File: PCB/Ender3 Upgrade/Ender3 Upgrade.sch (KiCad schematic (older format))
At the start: 1 part

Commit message: PCB Designed
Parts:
- added C1, C2, C3, C4, C5, C6, C7, C8: Conn_01x02, Connector_JST:JST_EH_B2B-EH-A_1x02_P2.50mm_Vertical, symbol Connector_Generic:Conn_01x02
- added DCDCBC2: DCDC 24-12, albe:BuckConverter, symbol Alberto:DCDCBuckConverter
- added J1, J2: Conn_01x04_Male, Connector_PinSocket_2.54mm:PinSocket_1x04_P2.54mm_Vertical, symbol Connector:Conn_01x04_Male
- added J3: Conn_01x02_Female, symbol Connector:Conn_01x02_Female
- added R1, R2, R3, R4, R5, R6, R7, R8: R1, Resistor_THT:R_Axial_DIN0204_L3.6mm_D1.6mm_P7.62mm_Horizontal, symbol Device:R
- added T1, T2, T3, T4, T5, T6, T7, T8: IRLZ34N, Package_TO_SOT_THT:TO-220-3_Vertical, symbol Transistor_FET:IRLZ34N
- DCDCBC1: value DCDCBuckConverter -> DCDC 24-5
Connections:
- net +24V: now also DCDCBC2.2 (IN+), J3.2 (Pin_2)
- net GND: now also DCDCBC1.3 (OUT-), DCDCBC2.3 (OUT-), R1.2, R2.2, R3.2, R4.2, R5.2, R6.2, R7.2, R8.2, T1.3 (S), T2.3 (S), T3.3 (S), T4.3 (S), T5.3 (S), T6.3 (S), T7.3 (S), T8.3 (S); no longer DCDCBC1.1 (IN-)
- net 5V: now reaches DCDCBC1.4 (OUT+)
- net 5V: now also C1.2 (Pin_2), C3.2 (Pin_2), C5.2 (Pin_2), C7.2 (Pin_2)
- new net: J1.4 (Pin_4), R1.1, T1.1 (G)
- new net: C1.1 (Pin_1), T1.2 (D)
- new net: C2.1 (Pin_1), T2.2 (D)
- new net: C4.1 (Pin_1), T4.2 (D)
- new net: C6.1 (Pin_1), T6.2 (D)
- new net: C8.1 (Pin_1), T8.2 (D)
- new net: J1.3 (Pin_3), R3.1, T3.1 (G)
- new net: C3.1 (Pin_1), T3.2 (D)
- new net: J1.2 (Pin_2), R5.1, T5.1 (G)
- new net: C5.1 (Pin_1), T5.2 (D)
- new net: J1.1 (Pin_1), R7.1, T7.1 (G)
- new net: C7.1 (Pin_1), T7.2 (D)
- new net: J2.4 (Pin_4), R8.1, T8.1 (G)
- new net: J2.3 (Pin_3), R6.1, T6.1 (G)
- new net: J2.2 (Pin_2), R4.1, T4.1 (G)
- new net: J2.1 (Pin_1), R2.1, T2.1 (G)
- new net 12V: C2.2 (Pin_2), C4.2 (Pin_2), C6.2 (Pin_2), C8.2 (Pin_2), DCDCBC2.4 (OUT+)
- new net GNDPWR: DCDCBC1.1 (IN-), DCDCBC2.1 (IN-), J3.1 (Pin_1)
- no-connect marks 0 -> 1

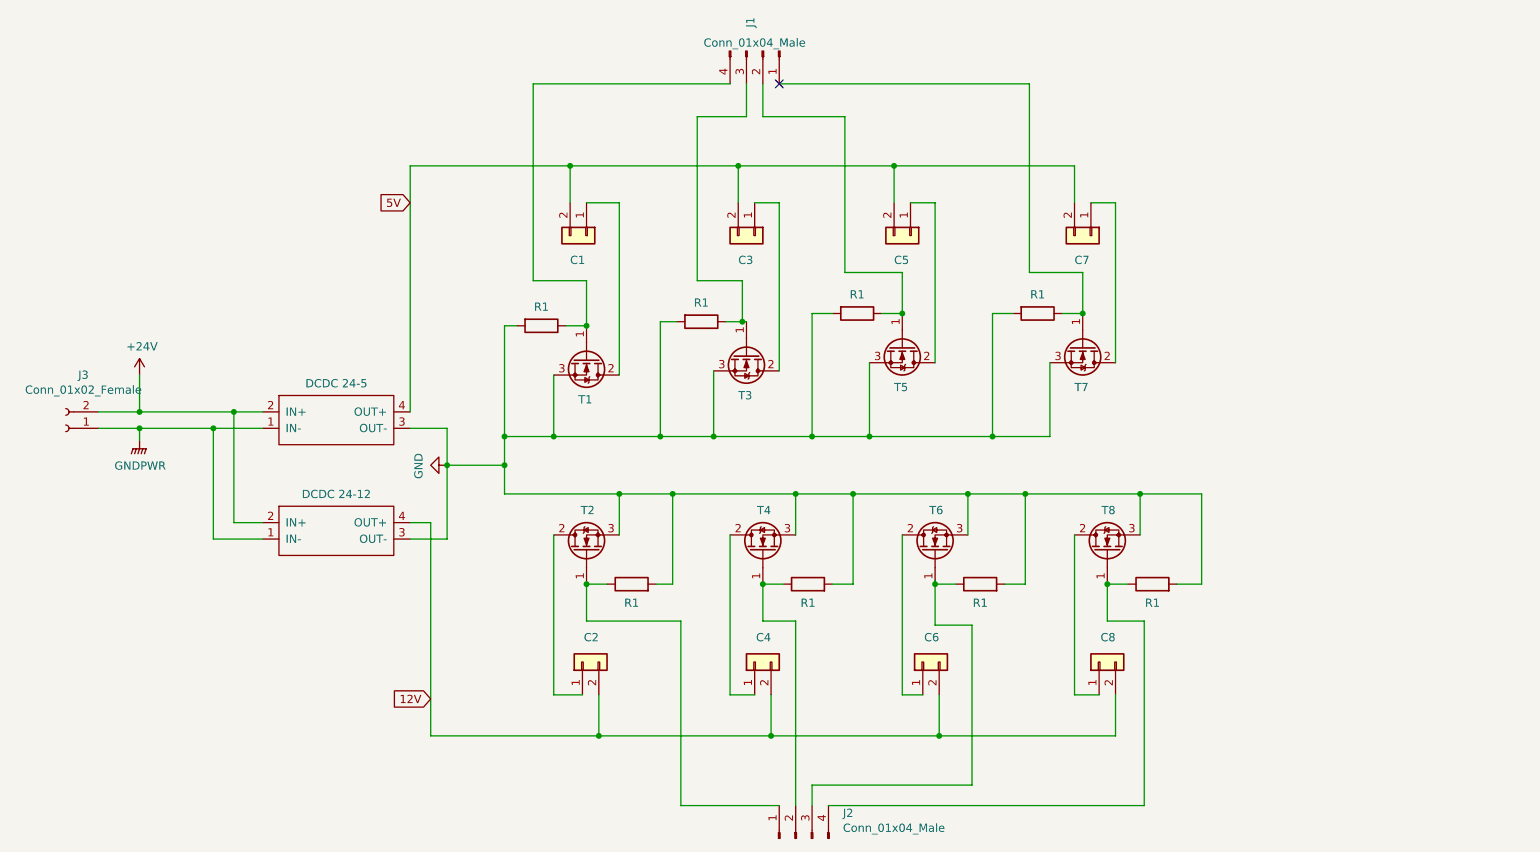
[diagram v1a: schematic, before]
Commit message: Drawers added
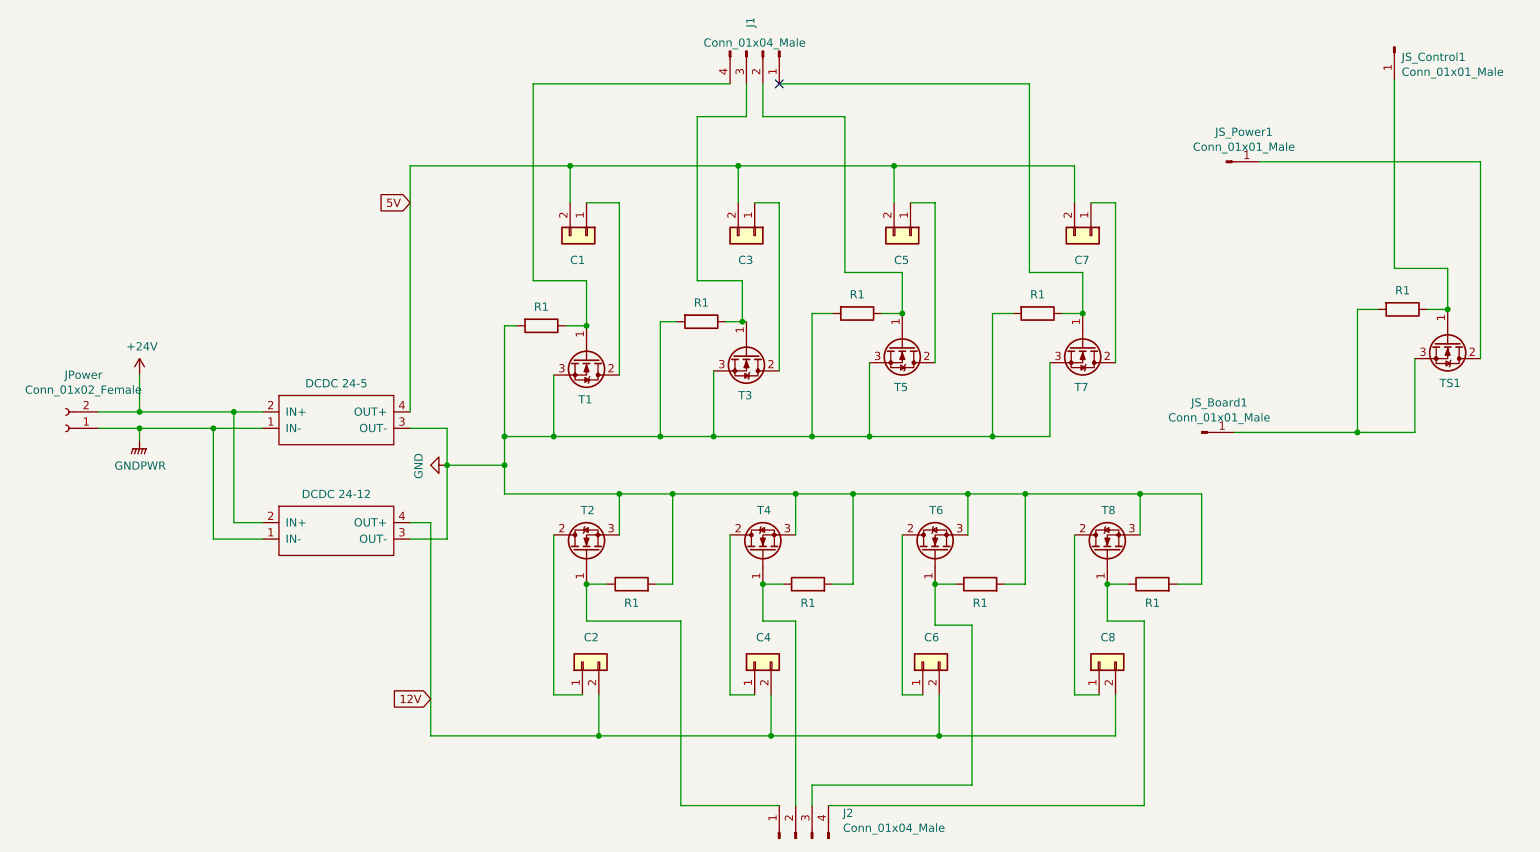
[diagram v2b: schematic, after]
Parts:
- removed J3: Conn_01x02_Female, symbol Connector:Conn_01x02_Female
- added JPower: Conn_01x02_Female, symbol Connector:Conn_01x02_Female
- added JS_Board1, JS_Control1, JS_Power1: Conn_01x01_Male, Connector_PinHeader_2.54mm:PinHeader_1x01_P2.54mm_Vertical, symbol Connector:Conn_01x01_Male
- added RS1: R1, Resistor_THT:R_Axial_DIN0204_L3.6mm_D1.6mm_P7.62mm_Horizontal, symbol Device:R
- added TS1: IRLZ34N, Package_TO_SOT_THT:TO-220-3_Vertical, symbol Transistor_FET:IRLZ34N
- J1, J2: footprint Connector_PinSocket_2.54mm:PinSocket_1x04_P2.54mm_Vertical -> Connector_PinHeader_2.54mm:PinHeader_1x04_P2.54mm_Vertical
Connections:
- net +24V: now also JPower.2 (Pin_2)
- net GNDPWR: now also JPower.1 (Pin_1)
- new net: JS_Power1.1 (Pin_1), TS1.2 (D)
- new net: JS_Board1.1 (Pin_1), RS1.2, TS1.3 (S)
- new net: JS_Control1.1 (Pin_1), RS1.1, TS1.1 (G)
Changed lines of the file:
@@
 F 0 "J2" V 5704 5712 50  0000 R CNN
 F 1 "Conn_01x04_Male" V 5613 5712 50  0000 R CNN
-F 2 "Connector_PinSocket_2.54mm:PinSocket_1x04_P2.54mm_Vertical" H 5550 6000 50  0001 C CNN
+F 2 "Connector_PinHeader_2.54mm:PinHeader_1x04_P2.54mm_Vertical" H 5550 6000 50  0001 C CNN
 F 3 "~" H 5550 6000 50  0001 C CNN
 	1    5550 6000
@@
 F 0 "J1" H 5175 1125 50  0000 C CNN
 F 1 "Conn_01x04_Male" V 5300 1150 50  0000 C CNN
-F 2 "Connector_PinSocket_2.54mm:PinSocket_1x04_P2.54mm_Vertical" H 5350 1200 50  0001 C CNN
+F 2 "Connector_PinHeader_2.54mm:PinHeader_1x04_P2.54mm_Vertical" H 5350 1200 50  0001 C CNN
 F 3 "~" H 5350 1200 50  0001 C CNN
 	1    5350 1200
@@
 	6975 1400 5450 1400
 Connection ~ 7300 2800
-$Comp
-L Connector:Conn_01x02_Female J3
-U 1 1 64084918
-P 1100 3500
-F 0 "J3" H 992 3175 50  0000 C CNN
-F 1 "Conn_01x02_Female" H 992 3266 50  0000 C CNN
-F 2 "" H 1100 3500 50  0001 C CNN
-F 3 "~" H 1100 3500 50  0001 C CNN
-	1    1100 3500
-	-1   0    0    1
-$EndComp
 Wire Wire Line
 	1300 3400 1550 3400
@@
 $EndComp
 NoConn ~ 5450 1400
+$Comp
+L Connector:Conn_01x01_Male JS_Power1
+U 1 1 6402B6DD
+P 8175 1875
+F 0 "JS_Power1" H 8283 2056 50  0000 C CNN
+F 1 "Conn_01x01_Male" H 8283 1965 50  0000 C CNN
+F 2 "Connector_PinHeader_2.54mm:PinHeader_1x01_P2.54mm_Vertical" H 8175 1875 50  0001 C CNN
+F 3 "~" H 8175 1875 50  0001 C CNN
+	1    8175 1875
+	1    0    0    -1
+$EndComp
+$Comp
+L Connector:Conn_01x01_Male JS_Board1
+U 1 1 64031B0D
+P 8025 3525
+F 0 "JS_Board1" H 8133 3706 50  0000 C CNN
+F 1 "Conn_01x01_Male" H 8133 3615 50  0000 C CNN
+F 2 "Connector_PinHeader_2.54mm:PinHeader_1x01_P2.54mm_Vertical" H 8025 3525 50  0001 C CNN
+F 3 "~" H 8025 3525 50  0001 C CNN
+	1    8025 3525
+	1    0    0    -1
+$EndComp
+$Comp
+L Transistor_FET:IRLZ34N TS1
+U 1 1 6403AD45
+P 9525 2975
+F 0 "TS1" V 9775 2925 50  0000 L CNN
+F 1 "IRLZ34N" H 9729 2930 50  0001 L CNN
+F 2 "Package_TO_SOT_THT:TO-220-3_Vertical" H 9775 2900 50  0001 L CIN
+F 3 "http://www.infineon.com/dgdl/irlz34npbf.pdf?fileId=5546d462533600a40153567206892720" H 9525 2975 50  0001 L CNN
+	1    9525 2975
+	0    1    1    0
+$EndComp
+$Comp
+L Device:R RS1
+U 1 1 6403B133
+P 9250 2775
+F 0 "RS1" V 9043 2775 50  0001 C CNN
+F 1 "R1" V 9135 2775 50  0000 C CNN
+F 2 "Resistor_THT:R_Axial_DIN0204_L3.6mm_D1.6mm_P7.62mm_Horizontal" V 9180 2775 50  0001 C CNN
+F 3 "~" H 9250 2775 50  0001 C CNN
+	1    9250 2775
+	0    1    1    0
+$EndComp
+Wire Wire Line
+	9525 2775 9400 2775
+Wire Wire Line
+	9325 3075 9325 3525
+Wire Wire Line
+	9325 3525 8975 3525
+Wire Wire Line
+	9100 2775 8975 2775
+Wire Wire Line
+	8975 2775 8975 3525
+Connection ~ 8975 3525
+Wire Wire Line
+	8975 3525 8225 3525
+Wire Wire Line
+	9525 2775 9525 2525
+Wire Wire Line
+	9525 2525 9200 2525
+Wire Wire Line
+	9200 2525 9200 1375
+Connection ~ 9525 2775
+$Comp
+L Connector:Conn_01x01_Male JS_Control1
+U 1 1 640540EF
+P 9200 1175
+F 0 "JS_Control1" V 9262 1219 50  0000 L CNN
+F 1 "Conn_01x01_Male" V 9353 1219 50  0000 L CNN
+F 2 "Connector_PinHeader_2.54mm:PinHeader_1x01_P2.54mm_Vertical" H 9200 1175 50  0001 C CNN
+F 3 "~" H 9200 1175 50  0001 C CNN
+	1    9200 1175
+	0    1    1    0
+$EndComp
+Wire Wire Line
+	8375 1875 9725 1875
+Wire Wire Line
+	9725 1875 9725 3075
+$Comp
+L Connector:Conn_01x02_Female JPower
+U 1 1 640A3D7F
+P 1100 3500
+F 0 "JPower" H 992 3175 50  0000 C CNN
+F 1 "Conn_01x02_Female" H 992 3266 50  0000 C CNN
+F 2 "" H 1100 3500 50  0001 C CNN
+F 3 "~" H 1100 3500 50  0001 C CNN
+	1    1100 3500
+	-1   0    0    1
+$EndComp
 $EndSCHEMATC
